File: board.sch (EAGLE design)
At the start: 86 parts, among them J1 XEM6310, U1 AD8022ARMZ, U2 AD5754BREZ, U3 ADR420ARZ, U4 LT1175CS8-5PBF, U5 LT1763CS8-5PBF, X1 LTI-SASF54GT, X2 LTI-SASF54GT, X5 LTI-SASF54GT, X6 LTI-SASF54GT, X7 LTI-SASF54GT, X8 LTI-SASF54GT

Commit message: Board/schematic consistency
Need input wiring now
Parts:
- added ADC2, ADC3: AD7357BRUZ, Analog Devices_By_element14_Batch_1:AD7357BRUZ
- added ADCOP3, ADCOP4, ADCOP5, ADCOP6: AD8138ARMZ, Analog Devices_By_element14_Batch_1:AD8138ARMZ
- added C37, C40, C42, C43, C45, C52, C53, C56, C57, C63, C65, C67, C69, C71, C73, C80, C81, C84, C85, C87, C89, C91, C93, C95, C97: 0.1uF, rcl:C-USC0603
- added C39, C41, C44, C50, C51, C54, C55, C62, C64, C66, C68, C70, C72, C78, C79, C82, C83, C86, C88, C90, C92, C94, C96: 10uF, rcl:CPOL-US
- added C46, C47, C48, C49, C74, C75, C76, C77: 39pF, rcl:C-USC0603
- added R21, R22, R27, R28, R37, R38, R43, R44: 33, resistor:R-US_R0603
- added R23, R24, R25, R26, R29, R30, R31, R32, R39, R40, R41, R42, R45, R46, R47, R48: 499, resistor:R-US_R0603
- added R33, R34, R35, R36, R49, R50, R51, R52: 10K, resistor:R-US_R0603
- added U6: AD5754BREZ, ADI-Phase-2:AD5754BREZ
- added U7: ADR420ARZ, Analog Devices_By_element14_Batch_1:ADR420ARZ
- added U8, U9: AD8022ARMZ, Analog Devices_By_element14_Batch_1:AD8022ARMZ
- added X10, X11, X12, X13, X14, X3, X4, X9: LTI-SASF54GT, con-coax:LTI-SASF54GT
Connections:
- removed net ADC4: J1.P$72
- removed net ADC5: J1.P$74
- removed net ADC6: J1.P$76
- new net ADC10: ADC2.SCLK
- new net ADC11: ADC3.~CS
- new net ADC12: ADC3.SDATAB
- new net ADC13: ADC3.SDATAA
- new net ADC14: ADC3.SCLK
- new net ADC7: ADC2.~CS
- new net ADC8: ADC2.SDATAB
- new net ADC9: ADC2.SDATAA
- new net DACD5: U6.SCLK
- new net DACD6: U6.LDAC
- new net DACD7: U6.SDIN
- new net DACD8: U6.CLR
- new net DACD9: U6.SYNC
- new net N$36: U6.VOUTD, X3.1
- new net N$42: U6.VOUTB, X9.1
- new net N$43: U6.VOUTC, X4.1
- new net N$45: U6.VOUTA, X10.1
- new net N$46: C37.2, U6.REFIN, U7.VOUT
- new net N$47: ADCOP3.-OUT, C46.2, R22.1, R24.2
- new net N$51: ADCOP3.-IN, C47.1, R23.1, R25.2
- new net N$52: ADCOP3.+IN, C46.1, R24.1, R26.2
- new net N$54: ADC2.VINA+, R21.2
- new net N$57: ADC2.VINA-, R22.2
- new net N$59: ADCOP3.+OUT, C47.2, R21.1, R23.2
- new net N$60: ADCOP4.-OUT, C48.2, R28.1, R30.2
- new net N$62: ADCOP4.-IN, C49.1, R29.1, R31.2
- new net N$63: ADCOP4.+IN, C48.1, R30.1, R32.2
- new net N$64: ADCOP4.+OUT, C49.2, R27.1, R29.2
- new net N$68: ADC2.VINB+, R27.2
- new net N$69: ADC2.VINB-, R28.2
- new net N$70: R32.1, X12.1
- new net N$71: R26.1, X11.1
- new net N$72: R33.1, U8.-IN2, U8.OUT2
- new net N$73: R34.1, U8.-IN1, U8.OUT1
- new net N$74: ADCOP3.VOCM, C57.2, R34.2, R36.2
- new net N$75: ADCOP4.VOCM, C56.1, R33.2, R35.1
- new net N$76: ADCOP5.-OUT, C74.2, R38.1, R40.2
- new net N$77: ADCOP5.-IN, C75.1, R39.1, R41.2
- new net N$78: ADCOP5.+IN, C74.1, R40.1, R42.2
- new net N$79: ADC3.VINA+, R37.2
- new net N$80: ADC3.VINA-, R38.2
- new net N$81: ADCOP5.+OUT, C75.2, R37.1, R39.2
- new net N$82: ADCOP6.-OUT, C76.2, R44.1, R46.2
- new net N$83: ADCOP6.-IN, C77.1, R45.1, R47.2
- new net N$84: ADCOP6.+IN, C76.1, R46.1, R48.2
- new net N$85: ADCOP6.+OUT, C77.2, R43.1, R45.2
- new net N$86: ADC3.VINB+, R43.2
- new net N$87: ADC3.VINB-, R44.2
- new net N$88: R48.1, X14.1
- new net N$89: R42.1, X13.1
- new net N$90: R49.1, U9.-IN2, U9.OUT2
- new net N$91: R50.1, U9.-IN1, U9.OUT1
- new net N$92: ADCOP5.VOCM, C85.2, R50.2, R52.2
- new net N$93: ADCOP6.VOCM, C84.1, R49.2, R51.1
- new net VREF2A: ADC2.REFA, C54.+, U8.+IN1
- new net VREF2B: ADC2.REFB, C55.+, U8.+IN2
- new net VREF3A: ADC3.REFA, C82.+, U9.+IN1
- new net VREF3B: ADC3.REFB, C83.+, U9.+IN2
- net +3V3: now also ADC2.VDR, ADC3.VDR, C44.+, C45.1, C51.+, C52.1, C79.+, C80.1, U6.DVCC
- net +5V: now also ADCOP3.V+, ADCOP4.V+, ADCOP5.V+, ADCOP6.V+, C39.+, C40.2, C43.1, C62.+, C63.2, C66.+, C67.2, C70.+, C71.2, C86.+, C87.2, C90.+, C91.2, C94.+, C95.2, U6.AVDD, U7.VIN, U8.+VS, U9.+VS
- net -5V: now also ADCOP3.V-, ADCOP4.V-, ADCOP5.V-, ADCOP6.V-, C41.-, C42.2, C64.-, C65.2, C68.-, C69.2, C72.-, C73.2, C88.-, C89.2, C92.-, C93.2, C96.-, C97.2, U6.AVSS, U8.-VS, U9.-VS
- net ADC0: now also J1.P$66; no longer J1.P$70
- net ADC1: now also J1.P$64; no longer J1.P$68
- net ADC2: now also J1.P$62; no longer J1.P$66
- net ADC3: now also J1.P$60; no longer J1.P$64
- net DACD0: now also J1.P$68; no longer J1.P$16
- net DACD1: now also J1.P$70; no longer J1.P$18
- net DACD2: now also J1.P$74; no longer J1.P$22
- net DACD3: now also J1.P$72; no longer J1.P$20
- net DACD4: now also J1.P$76; no longer J1.P$24
- net GND: now also ADC2.AGND, ADC2.AGND_2, ADC2.DGND, ADC2.REFGND, ADC3.AGND, ADC3.AGND_2, ADC3.DGND, ADC3.REFGND, C37.1, C39.-, C40.1, C41.+, C42.1, C43.2, C44.-, C45.2, C50.-, C51.-, C52.2, C53.2, C54.-, C55.-, C56.2, C57.1, C62.-, C63.1, C64.+, C65.1, C66.-, C67.1, C68.+, C69.1, C70.-, C71.1, C72.+, C73.1, C78.-, C79.-, C80.2, C81.2, C82.-, C83.-, C84.2, C85.1, C86.-, C87.1, C88.+, C89.1, C90.-, C91.1, C92.+, C93.1, C94.-, C95.1, C96.+, C97.1, R25.1, R31.1, R35.2, R36.1, R41.1, R47.1, R51.2, R52.1, U6.BIN/_2SCOMP, U6.DAC_GND, U6.DAC_GND_2, U6.GND, U6.SIG_GND, U6.SIG_GND_2, U7.GND, X10.2, X11.2, X12.2, X13.2, X14.2, X3.2, X4.2, X9.2
- net VDD: now also ADC2.VDD, ADC3.VDD, C50.+, C53.1, C78.+, C81.1
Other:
- note removed: "ADC Power"
- note removed: "DAC Power"
- note removed: "Main Power"
- moved on the sheet: C32, C38, U2, U3, X5, X6, X7, X8

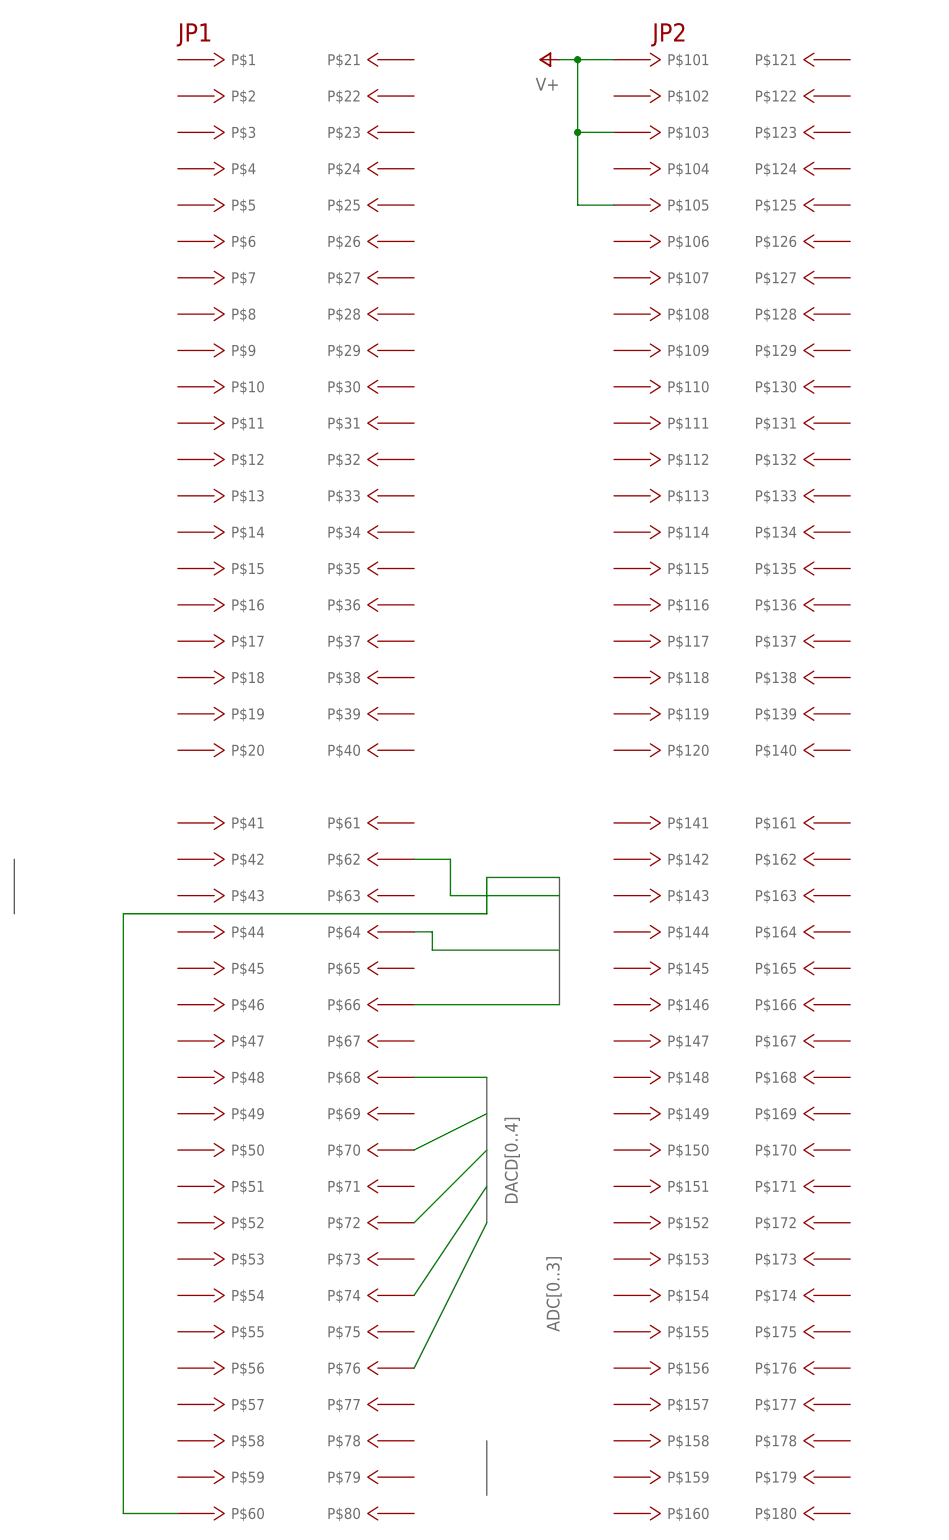
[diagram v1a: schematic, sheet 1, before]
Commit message: Routed signals
Need to fix SMA connector spacing
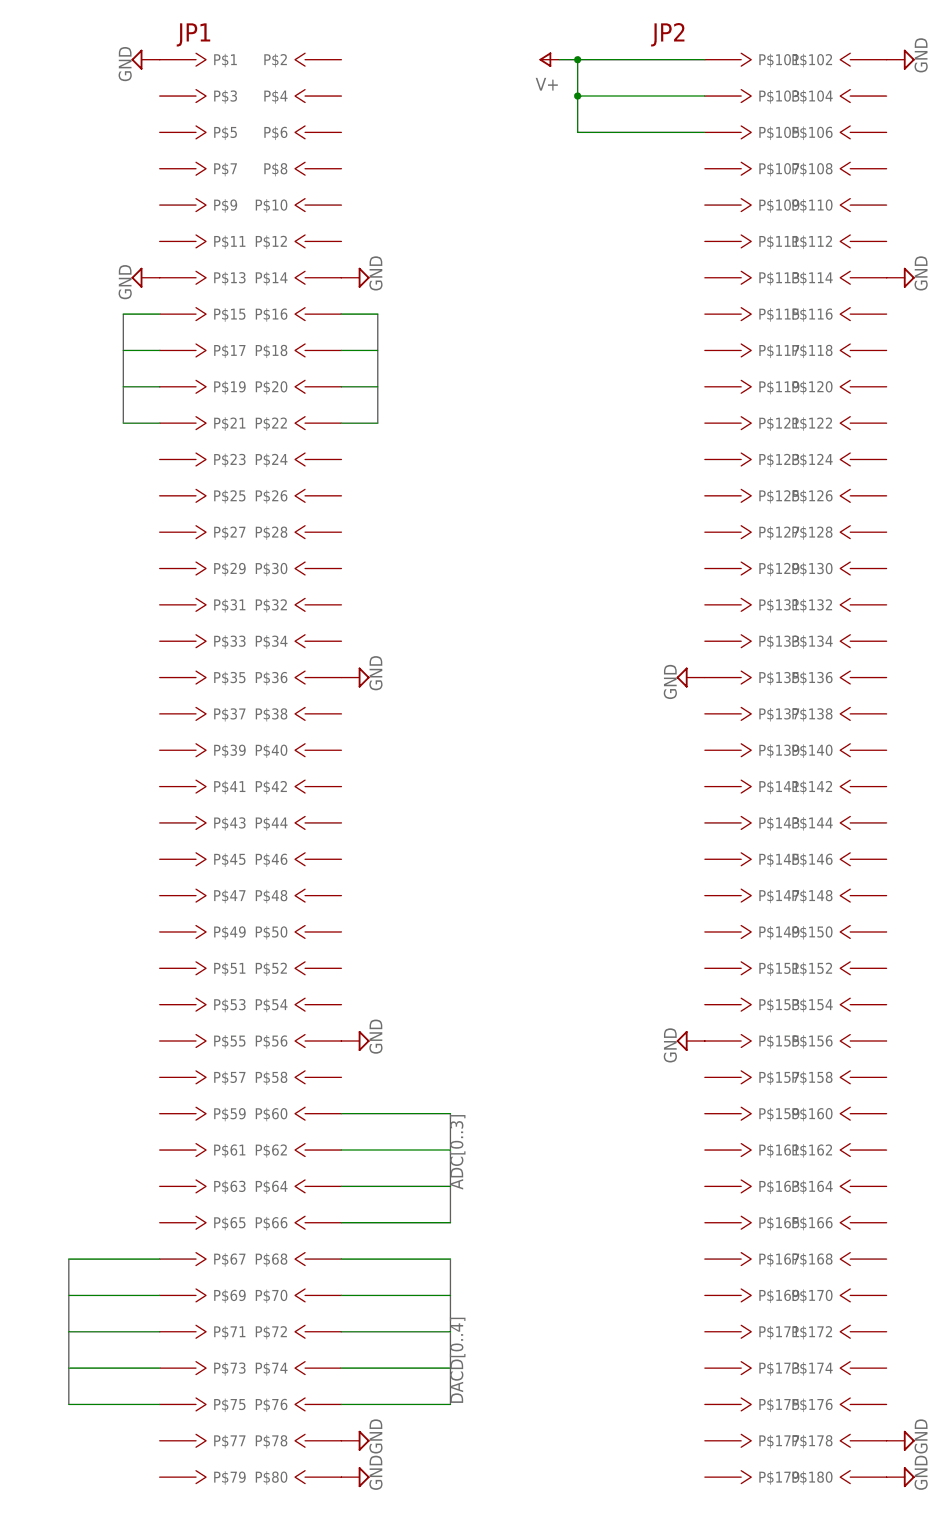
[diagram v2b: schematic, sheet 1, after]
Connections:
- new net N$94: U6.EP
- new net N$95: U2.EP
- net ADC10: now also J1.P$16
- net ADC11: now also J1.P$21
- net ADC12: now also J1.P$19
- net ADC13: now also J1.P$17
- net ADC14: now also J1.P$15
- net ADC7: now also J1.P$22
- net ADC8: now also J1.P$20
- net ADC9: now also J1.P$18
- net DACD2: now also J1.P$72, U2.SDIN; no longer J1.P$74, U2.LDAC
- net DACD3: now also J1.P$74, U2.LDAC; no longer J1.P$72, U2.SDIN
- net DACD5: now also J1.P$67, U6.SYNC; no longer U6.SCLK
- net DACD6: now also J1.P$69, U6.SCLK; no longer U6.LDAC
- net DACD7: now also J1.P$71
- net DACD8: now also J1.P$73, U6.LDAC; no longer U6.CLR
- net DACD9: now also J1.P$75, U6.CLR; no longer U6.SYNC
- net GND: now also J1.P$102, J1.P$114, J1.P$13, J1.P$135, J1.P$14, J1.P$155, J1.P$178, J1.P$180, J1.P$36, J1.P$56, J1.P$78, J1.P$80

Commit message: Fixed power
Added caps for all linear regulators
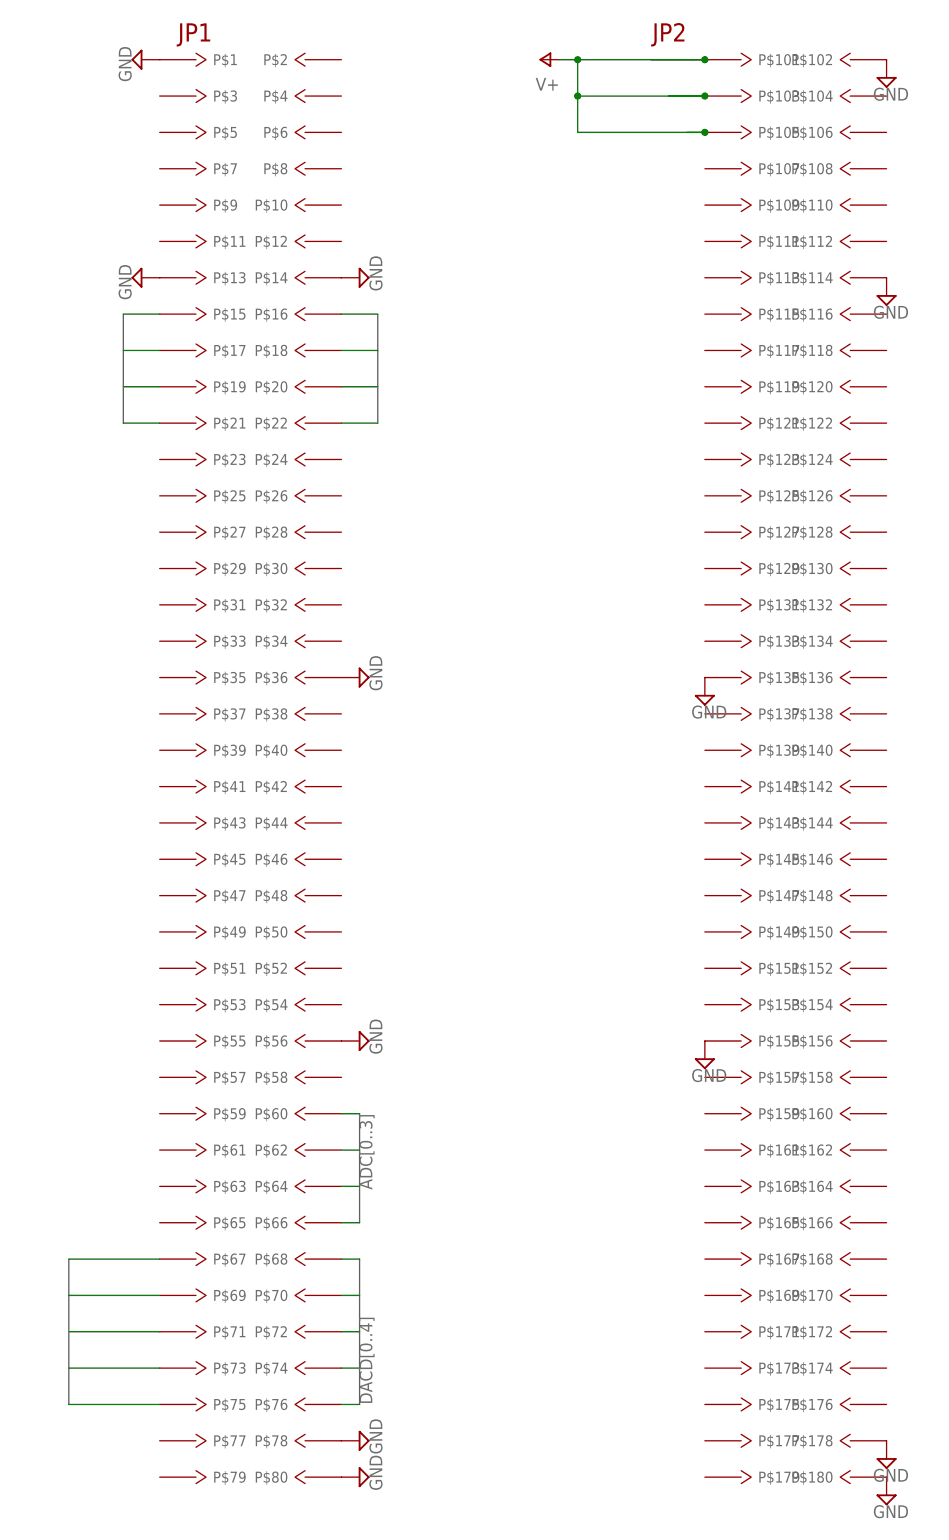
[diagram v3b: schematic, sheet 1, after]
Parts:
- added C100, C99: 4.7uF, rcl:C-USC0603
- added C98: 1uF Tant, rcl:CPOL-US
- C30: value 0.1uF Tant -> 4.7uF
- C35, C36: value (none) -> 100uF
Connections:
- net +3V3: now also C99.1
- net +5V: now also C30.1
- net GND: now also C100.2, C30.2, C98.+, C99.2, J1.P$1; no longer C30.1
- net N$66: now also C98.-; no longer C30.2
- net VDD: now also C100.1
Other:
- moved on the sheet: C30

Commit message: added some helpful pdfs
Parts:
- C35, C36: value 100uF -> 47uF
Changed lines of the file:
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@@
 <part name="P-7" library="supply1" deviceset="-5V" device=""/>
 <part name="GND16" library="supply2" deviceset="GND" device=""/>
-<part name="C35" library="rcl" deviceset="CPOL-US" device="UD-4X5,8" value="100uF"/>
-<part name="C36" library="rcl" deviceset="CPOL-US" device="UD-4X5,8" value="100uF"/>
+<part name="C35" library="rcl" deviceset="CPOL-US" device="UD-4X5,8" value="47uF"/>
+<part name="C36" library="rcl" deviceset="CPOL-US" device="UD-4X5,8" value="47uF"/>
 <part name="+3V2" library="supply1" deviceset="+3V3" device=""/>
 <part name="U6" library="ADI-Phase-2" deviceset="AD5754BREZ" device=""/>
